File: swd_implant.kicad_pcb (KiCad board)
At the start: 2 copper layers, 13.9 x 39 mm, 25 parts, among them J1 U262-161N-4BVC11, J2 G&W pressure contact, J3 50 mil Pin Header, J4 SOICbite, J5 100 mil Pin Header, J6 100 mil Pin header, U1 ATSAMD21E18A, U2 AP2127K-3.3

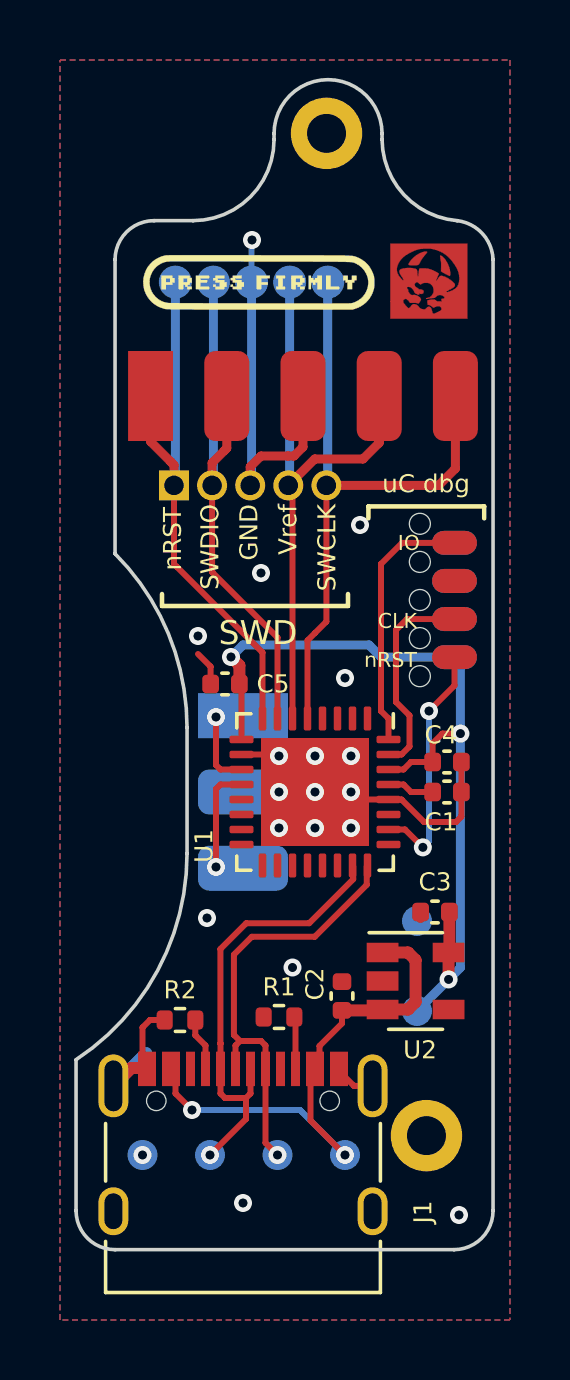
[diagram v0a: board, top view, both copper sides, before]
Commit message: 0.5mm shorter; added test points for UART
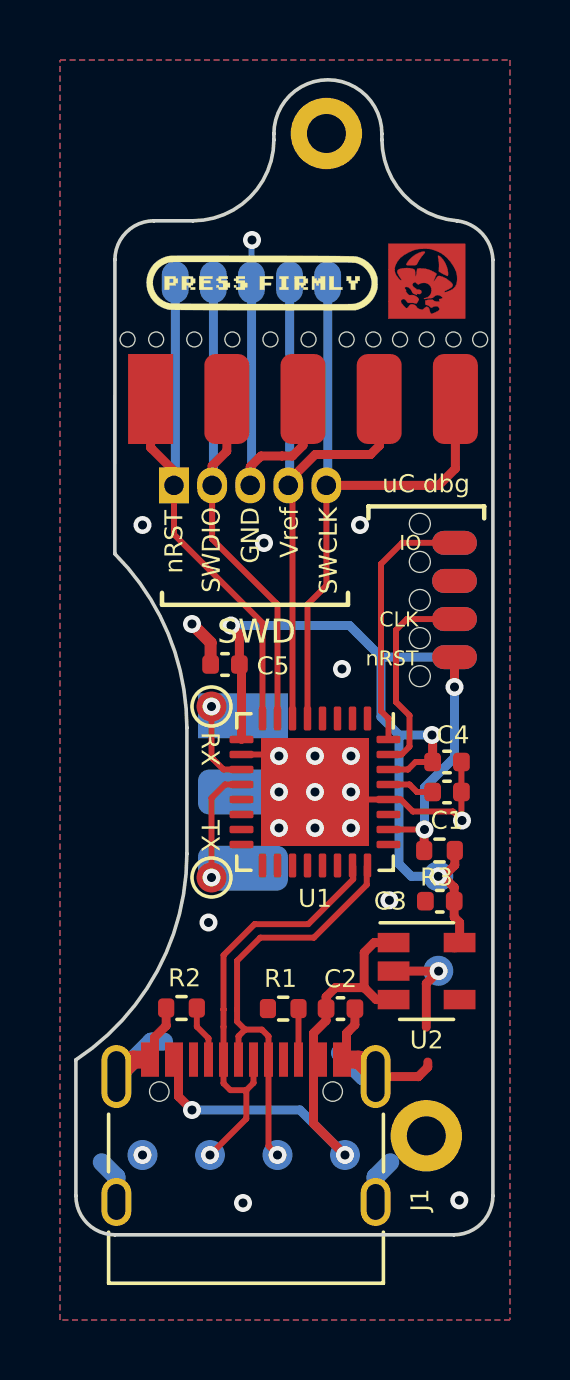
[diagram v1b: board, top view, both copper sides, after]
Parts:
- added R3: 10k, Resistor_SMD:R_0402_1005Metric, F.Cu at (64.7, 118.8)
- added TP7: TP_USB_D+, GnW_SWD:TestPoint_Pad_D1.0mm, F.Cu at (57.0, 114.0)
- added TP8: TP_USB_D+, GnW_SWD:TestPoint_Pad_D1.0mm, F.Cu at (57.0, 119.8)
- J3: footprint Connector_PinHeader_1.27mm:PinHeader_1x05_P1.27mm_Vertical -> GnW_SWD:PinHeader_1x05_P1.27mm_Vertical
- TP1, TP2, TP3, TP4, TP5, TP6: footprint TestPoint:TestPoint_Pad_D1.0mm -> GnW_SWD:TestPoint_Pad_D1.0mm
- moved J2 8.90 mm to (60.9, 93.2)
- moved TP4 4.55 mm to (64.6, 119.7)
- moved TP6 1.81 mm to (64.6, 122.9)
- moved Ref** 1.51 mm to (59.2, 123.0)
- moved C5 0.65 mm to (57.5, 112.7)
- moved Ref** 0.53 mm to (60.1, 104.3)
- moved U2 0.49 mm to (64.2, 122.9)
- moved C2 0.42 mm to (61.4, 124.1), turned to 180 degrees
- moved R2 0.40 mm to (56.0, 124.1)
- moved C3 0.39 mm to (64.7, 120.5)
- moved J1 0.33 mm to (58.2, 129.5)
- moved R1 0.31 mm to (59.4, 124.1)
- moved Ref** 0.11 mm to (58.7, 99.9)
- moved J5 0.10 mm to (60.1, 105.3)
- moved Ref** 0.07 mm to (64.2, 99.9)
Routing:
- net GND: track 35.1 -> 48.5 mm, vias 19 -> 22
- net VCC: track 28.7 -> 27.9 mm
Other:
- board size 13.9 x 39 mm -> 13.9 x 38.5 mm
